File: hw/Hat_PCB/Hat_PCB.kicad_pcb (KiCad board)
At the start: 2 copper layers, 65 x 56 mm, 63 parts, among them J1 EE_WP, J10 AudioJack3, J11 AudioJack3_Ground, J2 40HAT, J3 AVR-ISP-6, J4 I2C, J5 RPi_Power, J6 AUD_IN, J7 OUT_SPK_L, J8 OUT_SPK_R, J9 CAP_TOUCH, Q1 DMMT5401, Q2 DMG2305UX, U1 CAT24C32, U2 ATtiny87-MU, U3 NCP1117-3.3_SOT223, U4 TSL2591, U5 BME680, U6 DS3231M, U7 TPA2016D2RTJR, U8 MPR121QR2

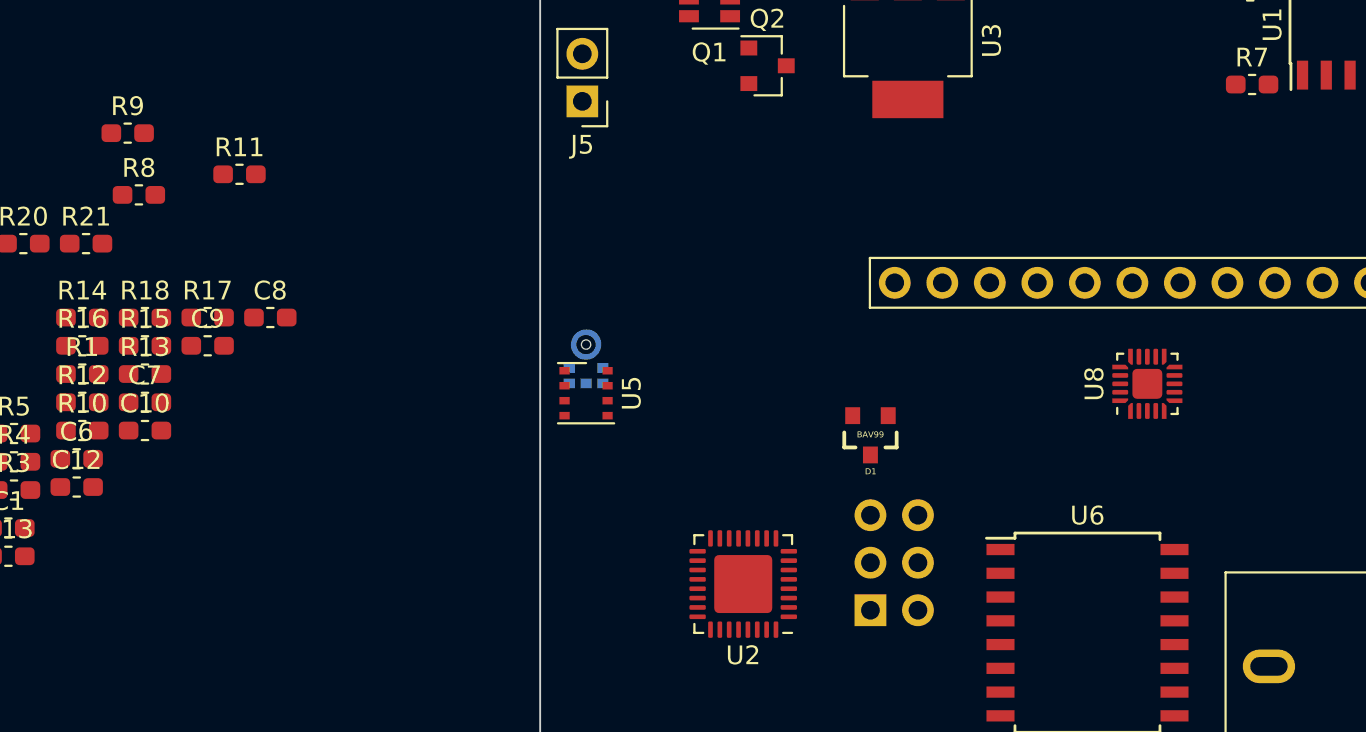
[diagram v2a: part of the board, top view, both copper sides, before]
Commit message: Added pull ups, LEDs, & swapped out cap touch IC
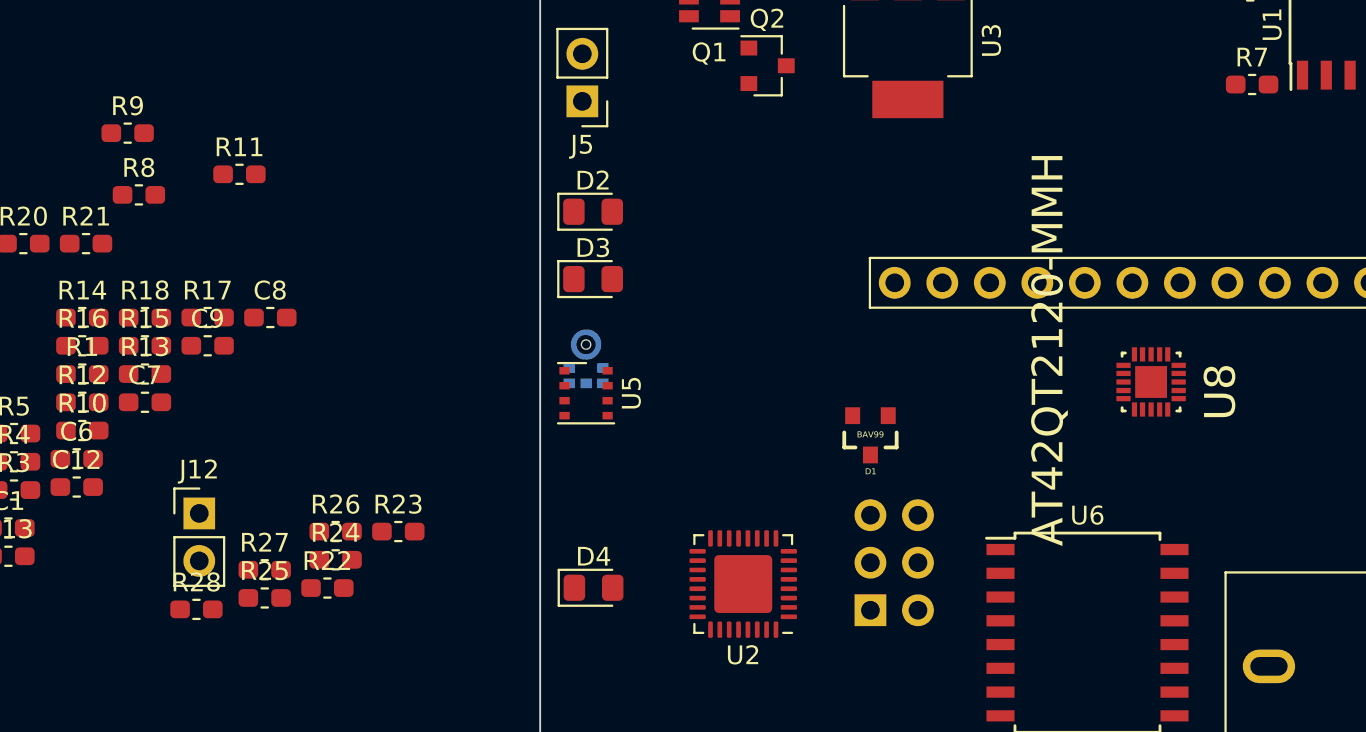
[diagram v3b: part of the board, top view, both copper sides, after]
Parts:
- removed C10: 0.1uF, Capacitor_SMD:C_0603_1608Metric_Pad1.05x0.95mm_HandSolder
- added D2: 5V_LED, Diode_SMD:D_0805_2012Metric_Pad1.15x1.40mm_HandSolder, F.Cu at (81.4, 81.0)
- added D3: 3V3_LED, Diode_SMD:D_0805_2012Metric_Pad1.15x1.40mm_HandSolder, F.Cu at (81.4, 84.6)
- added D4: GPIO_LED, Diode_SMD:D_0805_2012Metric_Pad1.15x1.40mm_HandSolder, F.Cu at (81.4, 101.1)
- added J12: I2C, Connector_PinHeader_2.54mm:PinHeader_1x02_P2.54mm_Vertical, F.Cu at (60.3, 97.1)
- added R22: 330R, Resistor_SMD:R_0603_1608Metric_Pad1.05x0.95mm_HandSolder, F.Cu at (67.2, 101.1)
- added R23: 10K, Resistor_SMD:R_0603_1608Metric_Pad1.05x0.95mm_HandSolder, F.Cu at (71.0, 98.1)
- added R24: 33R, Resistor_SMD:R_0603_1608Metric_Pad1.05x0.95mm_HandSolder, F.Cu at (67.6, 99.6)
- added R25: 33R, Resistor_SMD:R_0603_1608Metric_Pad1.05x0.95mm_HandSolder, F.Cu at (63.8, 101.6)
- added R26: 3.9K, Resistor_SMD:R_0603_1608Metric_Pad1.05x0.95mm_HandSolder, F.Cu at (67.6, 98.1)
- added R27: 3.9K, Resistor_SMD:R_0603_1608Metric_Pad1.05x0.95mm_HandSolder, F.Cu at (63.8, 100.1)
- added R28: 47K, Resistor_SMD:R_0603_1608Metric_Pad1.05x0.95mm_HandSolder, F.Cu at (60.2, 102.3)
- J4: value I2C -> ID_I2C
- R20: value 75K -> 330R
- R5: value 10K -> 330R
- U8: value MPR121QR2 -> AT42QT2120-MMH; footprint Package_DFN_QFN:QFN-20-1EP_3x3mm_P0.45mm_EP1.6x1.6mm -> QFN45P300X300X85-21N
- moved U8 0.22 mm to (111.2, 90.1)
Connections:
- R20 pad 1: Net-(R20-Pad1) -> GND
- R20 pad 2: GND -> Net-(D3-Pad1)
- R21 pad 2: /CAP_IRQ -> Net-(R21-Pad2)
- R5 pad 1: +3V3 -> GND
- R5 pad 2: Net-(J1-Pad2) -> Net-(D2-Pad1)
- U8 pad 1: /CAP_IRQ -> Net-(J9-Pad7)
- U8 pad 10: Net-(J9-Pad3) -> GND
- U8 pad 11: Net-(J9-Pad4) -> /SCL
- U8 pad 12: Net-(J9-Pad5) -> Net-(R21-Pad2)
- U8 pad 13: Net-(J9-Pad6) -> Net-(U8-Pad13)
- U8 pad 14: Net-(J9-Pad7) -> /SDA
- U8 pad 15: Net-(J9-Pad8) -> Net-(R28-Pad2)
- U8 pad 16: Net-(J9-Pad9) -> Net-(J9-Pad12)
- U8 pad 17: Net-(J9-Pad10) -> Net-(J9-Pad11)
- U8 pad 18: Net-(J9-Pad11) -> Net-(J9-Pad10)
- U8 pad 19: Net-(J9-Pad12) -> Net-(J9-Pad9)
- U8 pad 2: /SCL -> Net-(J9-Pad6)
- U8 pad 20: +3V3 -> Net-(J9-Pad8)
- U8 pad 21: (no net) -> GND
- U8 pad 3: /SDA -> Net-(J9-Pad5)
- U8 pad 4: GND -> Net-(J9-Pad4)
- U8 pad 5: Net-(C10-Pad1) -> Net-(J9-Pad3)
- U8 pad 6: GND -> Net-(J9-Pad2)
- U8 pad 7: Net-(R20-Pad1) -> Net-(J9-Pad1)
- U8 pad 8: Net-(J9-Pad1) -> GND
- U8 pad 9: Net-(J9-Pad2) -> +3V3

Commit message: change back RTC, finish placement mostly
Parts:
- added J13: LED_Out, TerminalBlock_Phoenix:TerminalBlock_Phoenix_MPT-0,5-2-2.54_1x02_P2.54mm_Horizontal, F.Cu at (89.1, 113.2)
- J2: moved to B.Cu
- J3: moved to F.Cu
- J5: footprint Connector_PinHeader_2.54mm:PinHeader_1x02_P2.54mm_Vertical -> TerminalBlock_Phoenix:TerminalBlock_Phoenix_MPT-0,5-2-2.54_1x02_P2.54mm_Horizontal
- moved R19 93.1 mm to (138.1, 104.6)
- moved C11 90.8 mm to (137.1, 108.8), turned to 270 degrees
- moved R18 83.0 mm to (138.1, 106.2), turned to 180 degrees
- moved C13 79.5 mm to (129.4, 104.9)
- moved C12 79.2 mm to (130.8, 114.1)
- moved R16 79.1 mm to (132.7, 79.1), turned to 90 degrees
- moved R13 79.0 mm to (136.4, 86.3)
- moved R15 79.0 mm to (136.4, 87.9), turned to 180 degrees
- moved R4 78.5 mm to (125.4, 71.0), turned to 270 degrees
- moved C8 72.5 mm to (136.4, 92.0)
- moved R17 70.6 mm to (129.4, 103.3)
- moved R2 68.1 mm to (108.8, 69.9), turned to 90 degrees
- moved R3 66.6 mm to (111.7, 69.8), turned to 90 degrees
- moved R21 63.0 mm to (116.8, 90.1), turned to 90 degrees
- moved R28 60.8 mm to (119.7, 90.1), turned to 90 degrees
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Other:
- board text added: "3V3"
- board text added: "5V"
- board text added: "AUD_IN"
- board text added: "AUD_LO"
- board text added: "AUD_RO"
- board text added: "EE_WP"
- board text added: "I2C"
- board text added: "ICSP"
- board text added: "ID_I2C"
- board text added: "LED_OUT"
- board text added: "LED_PB1"
- board text added: "PWR"
